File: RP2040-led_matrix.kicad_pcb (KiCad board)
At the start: 2 copper layers, 187 parts, among them J2 USB_C_Receptacle, Q1 BSS84, Q10 BSS84, Q11 2N7002, Q12 2N7002, Q13 2N7002, Q14 2N7002, Q15 2N7002, Q16 2N7002, Q17 2N7002, Q18 2N7002, Q19 2N7002, Q2 BSS84, Q20 2N7002, Q3 BSS84, Q4 BSS84, Q5 BSS84, Q6 BSS84, Q7 BSS84, Q8 BSS84, Q9 BSS84, SW2 SW_DIP_x01, U1 W25Q16JVSS, U2 RP2040, U4 NCP1117-1.5_SOT223, Y2 ABM8-272-T3

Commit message: improved design of the matrix
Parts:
- removed C17, C18: 100n, Capacitor_SMD:C_0603_1608Metric
- removed J2: USB_C_Receptacle, Connector_USB:USB_C_Receptacle_GCT_USB4110
- removed SW2: SW_DIP_x01, Button_Switch_SMD:SW_DIP_SPSTx01_Slide_6.7x4.1mm_W6.73mm_P2.54mm_LowProfile_JPin
- removed U4: NCP1117-1.5_SOT223, Package_TO_SOT_SMD:SOT-223-3_TabPin2
- removed Y2: ABM8-272-T3, Crystal:Crystal_SMD_3225-4Pin_3.2x2.5mm
- added C1: 15p, Capacitor_SMD:C_0603_1608Metric, F.Cu at (117.7, 16.4)
- added C2: 15p, Capacitor_SMD:C_0603_1608Metric, F.Cu at (117.7, 18.9)
- added J1: USB_C_Receptacle, Connector_USB:USB_C_Receptacle_GCT_USB4110, F.Cu at (165.0, 50.0)
- added R46: 100, Resistor_SMD:R_0603_1608Metric, F.Cu at (101.7, 16.9)
- added R47: 100, Resistor_SMD:R_0603_1608Metric, F.Cu at (101.7, 19.4)
- added R48: 100, Resistor_SMD:R_0603_1608Metric, F.Cu at (101.7, 21.9)
- added R49: 100, Resistor_SMD:R_0603_1608Metric, F.Cu at (101.7, 24.4)
- added R50: 100, Resistor_SMD:R_0603_1608Metric, F.Cu at (101.7, 27.0)
- added R51: 100, Resistor_SMD:R_0603_1608Metric, F.Cu at (101.7, 29.5)
- added R52: 100, Resistor_SMD:R_0603_1608Metric, F.Cu at (101.7, 32.0)
- added R53: 100, Resistor_SMD:R_0603_1608Metric, F.Cu at (101.7, 34.5)
- added R54: 100, Resistor_SMD:R_0603_1608Metric, F.Cu at (101.7, 37.0)
- added R55: 100, Resistor_SMD:R_0603_1608Metric, F.Cu at (101.7, 39.5)
- added SW1: SW_DIP_x01, Button_Switch_SMD:SW_DIP_SPSTx01_Slide_6.7x4.1mm_W6.73mm_P2.54mm_LowProfile_JPin, F.Cu at (176.0, 63.0)
- added U3: W25Q16JVSS, Package_SO:SOIC-8_5.3x5.3mm_P1.27mm, F.Cu at (152.5, 63.0)
- added Y1: ABM8-272-T3, Crystal:Crystal_SMD_3225-4Pin_3.2x2.5mm, F.Cu at (174.4, 74.3)
- C10, C9: value 10u -> 100n
- C13, C14, C15: value 100n -> 10u
- C3: value 1u -> 10u
- C4: value 1u -> 100n
- C6, C7: value 15p -> 100n
- R1: value 1k -> 5.1k
- R12, R18, R24, R33: value 100 -> 47
- R13, R19, R25, R28, R31, R34: value 100k -> 100
- R14, R20, R26, R29, R32, R36, R37, R40, R41, R44, R45, R8: value 100 -> 100k
- R15, R21, R27, R30, R9: value 100k -> 47
- R2: value 100 -> 5.1k
- R3: value 100k -> 1k
- R4: value 10k -> 1k
- R5: value 1k -> 100k
- R6: value 5.1k -> 47
- R7: value 5.1k -> 100
- U1: value W25Q16JVSS -> RP2040; footprint Package_SO:SOIC-8_5.3x5.3mm_P1.27mm -> Package_DFN_QFN:QFN-56-1EP_7x7mm_P0.4mm_EP3.2x3.2mm
- U2: value RP2040 -> NCP1117-1.5_SOT223; footprint Package_DFN_QFN:QFN-56-1EP_7x7mm_P0.4mm_EP3.2x3.2mm -> Package_TO_SOT_SMD:SOT-223-3_TabPin2
- moved R6 103.6 mm to (85.6, 16.9)
- moved R7 103.6 mm to (85.6, 19.4)
- moved D1 87.6 mm to (30.0, 25.8)
- moved D10 87.6 mm to (30.0, 49.1)
- moved D100 87.6 mm to (58.3, 46.5)
- moved D11 87.6 mm to (30.0, 51.7)
- moved D12 87.6 mm to (30.0, 54.3)
- moved D13 87.6 mm to (30.0, 56.9)
- moved D14 87.6 mm to (34.0, 25.8)
- moved D15 87.6 mm to (34.0, 28.4)
- moved D16 87.6 mm to (34.0, 31.0)
- moved D17 87.6 mm to (34.0, 33.6)
- moved D18 87.6 mm to (34.0, 36.2)
- moved D19 87.6 mm to (34.0, 38.7)
- moved D2 87.6 mm to (30.0, 28.4)
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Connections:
- C14 pad 1: +3.3V -> +5V
- C16 pad 1: +3.3V -> GND
- C16 pad 2: GND -> +3.3V
- C3 pad 1: +3.3V -> GND
- C3 pad 2: GND -> +1V1
- C6 pad 1: Net-(U2-XIN) -> +3.3V
- C7 pad 1: Net-(C7-Pad1) -> +3.3V
- C8 pad 1: GND -> +3.3V
- C8 pad 2: +3.3V -> GND
- C9 pad 1: +5V -> +3.3V
- Q1 pad 2: +5V -> Net-(Q1-S)
- Q10 pad 2: +5V -> Net-(Q10-S)
- Q2 pad 2: +5V -> Net-(Q2-S)
- Q3 pad 2: +5V -> Net-(Q3-S)
- Q4 pad 2: +5V -> Net-(Q4-S)
- Q5 pad 2: +5V -> Net-(Q5-S)
- Q6 pad 2: +5V -> Net-(Q6-S)
- Q7 pad 2: +5V -> Net-(Q7-S)
- Q8 pad 2: +5V -> Net-(Q8-S)
- Q9 pad 2: +5V -> Net-(Q9-S)
- R1 pad 2: /QSPI_SS -> GND
- R10 pad 1: C3 -> C2
- R10 pad 2: Net-(Q3-G) -> Net-(Q2-G)
- R11 pad 1: Net-(Q3-G) -> Net-(Q2-G)
- R11 pad 2: +5V -> Net-(Q2-S)
- R12 pad 1: R1 -> +3.3V
- R12 pad 2: Net-(Q11-G) -> Net-(Q3-S)
- R13 pad 1: Net-(Q11-G) -> C3
- R13 pad 2: GND -> Net-(Q3-G)
- R14 pad 1: C4 -> Net-(Q3-G)
- R14 pad 2: Net-(Q4-G) -> Net-(Q3-S)
- R15 pad 1: Net-(Q4-G) -> +3.3V
- R15 pad 2: +5V -> Net-(Q4-S)
- R16 pad 1: C5 -> C4
- R16 pad 2: Net-(Q5-G) -> Net-(Q4-G)
- R17 pad 1: Net-(Q5-G) -> Net-(Q4-G)
- R17 pad 2: +5V -> Net-(Q4-S)
- R18 pad 1: C6 -> +3.3V
- R18 pad 2: Net-(Q6-G) -> Net-(Q5-S)
- R19 pad 1: Net-(Q6-G) -> C5
- R19 pad 2: +5V -> Net-(Q5-G)
- R2 pad 1: C1 -> Net-(J1-CC2)
- R2 pad 2: Net-(Q1-G) -> GND
- R20 pad 1: C7 -> Net-(Q5-G)
- R20 pad 2: Net-(Q7-G) -> Net-(Q5-S)
- R21 pad 1: Net-(Q7-G) -> +3.3V
- R21 pad 2: +5V -> Net-(Q6-S)
- R22 pad 1: C8 -> C6
- R22 pad 2: Net-(Q8-G) -> Net-(Q6-G)
- R23 pad 1: Net-(Q8-G) -> Net-(Q6-G)
- R23 pad 2: +5V -> Net-(Q6-S)
- R24 pad 1: C9 -> +3.3V
- R24 pad 2: Net-(Q9-G) -> Net-(Q7-S)
- R25 pad 1: Net-(Q9-G) -> C7
- R25 pad 2: +5V -> Net-(Q7-G)
- R26 pad 1: C10 -> Net-(Q7-G)
- R26 pad 2: Net-(Q10-G) -> Net-(Q7-S)
- R27 pad 1: Net-(Q10-G) -> +3.3V
- R27 pad 2: +5V -> Net-(Q8-S)
- R28 pad 1: Net-(Q12-G) -> C8
- R28 pad 2: GND -> Net-(Q8-G)
- R29 pad 1: R2 -> Net-(Q8-G)
- R29 pad 2: Net-(Q12-G) -> Net-(Q8-S)
- R3 pad 1: Net-(Q1-G) -> Net-(U1-XOUT)
- R3 pad 2: +5V -> Net-(C2-Pad1)
- R30 pad 1: Net-(Q13-G) -> +3.3V
- R30 pad 2: GND -> Net-(Q9-S)
- R31 pad 1: Net-(Q14-G) -> C9
- R31 pad 2: GND -> Net-(Q9-G)
- R32 pad 1: R3 -> Net-(Q9-G)
- R32 pad 2: Net-(Q13-G) -> Net-(Q9-S)
- R33 pad 1: R4 -> +3.3V
- R33 pad 2: Net-(Q14-G) -> Net-(Q10-S)
- R34 pad 1: Net-(Q15-G) -> C10
- R34 pad 2: GND -> Net-(Q10-G)
- R35 pad 1: Net-(Q16-G) -> Net-(Q10-G)
- R35 pad 2: GND -> Net-(Q10-S)
- R36 pad 1: R5 -> Net-(Q11-G)
- R36 pad 2: Net-(Q15-G) -> GND
- R37 pad 1: R6 -> Net-(Q12-G)
- R37 pad 2: Net-(Q16-G) -> GND
- R38 pad 1: Net-(Q17-G) -> Net-(Q13-G)
- R39 pad 1: Net-(Q18-G) -> Net-(Q14-G)
- R4 pad 1: /QSPI_SS -> Net-(R4-Pad1)
- R4 pad 2: +3.3V -> /QSPI_SS
- R40 pad 1: R7 -> Net-(Q15-G)
- R40 pad 2: Net-(Q17-G) -> GND
- R41 pad 1: R8 -> Net-(Q16-G)
- R41 pad 2: Net-(Q18-G) -> GND
- R42 pad 1: Net-(Q19-G) -> Net-(Q17-G)
- R43 pad 1: Net-(Q20-G) -> Net-(Q18-G)
- R44 pad 1: R9 -> Net-(Q19-G)
- R44 pad 2: Net-(Q19-G) -> GND
- R45 pad 1: R10 -> Net-(Q20-G)
- R45 pad 2: Net-(Q20-G) -> GND
- R5 pad 1: Net-(U2-XOUT) -> /QSPI_SS
- R5 pad 2: Net-(C7-Pad1) -> +3.3V
- R6 pad 1: Net-(J2-CC1) -> +3.3V
- R6 pad 2: GND -> Net-(Q1-S)
- R7 pad 1: Net-(J2-CC2) -> C1
- R7 pad 2: GND -> Net-(Q1-G)
- R8 pad 1: C2 -> Net-(Q1-G)
- R8 pad 2: Net-(Q2-G) -> Net-(Q1-S)
- R9 pad 1: Net-(Q2-G) -> +3.3V
- R9 pad 2: +5V -> Net-(Q2-S)
- U1 pad 1: /QSPI_SS -> +3.3V
- U1 pad 2: /QSPI_SD1 -> unconnected-(U1-GPIO0-Pad2)
- U1 pad 3: /QSPI_SD2 -> C1
- U1 pad 4: GND -> C2
- U1 pad 5: /QSPI_SD0 -> C3
- U1 pad 6: /QSPI_SCLK -> C4
- U1 pad 7: /QSPI_SD3 -> C5
- U1 pad 8: +3.3V -> C6
- U2 pad 1: +3.3V -> GND
- U2 pad 2: unconnected-(U2-GPIO0-Pad2) -> +3.3V
- U2 pad 3: C1 -> +5V

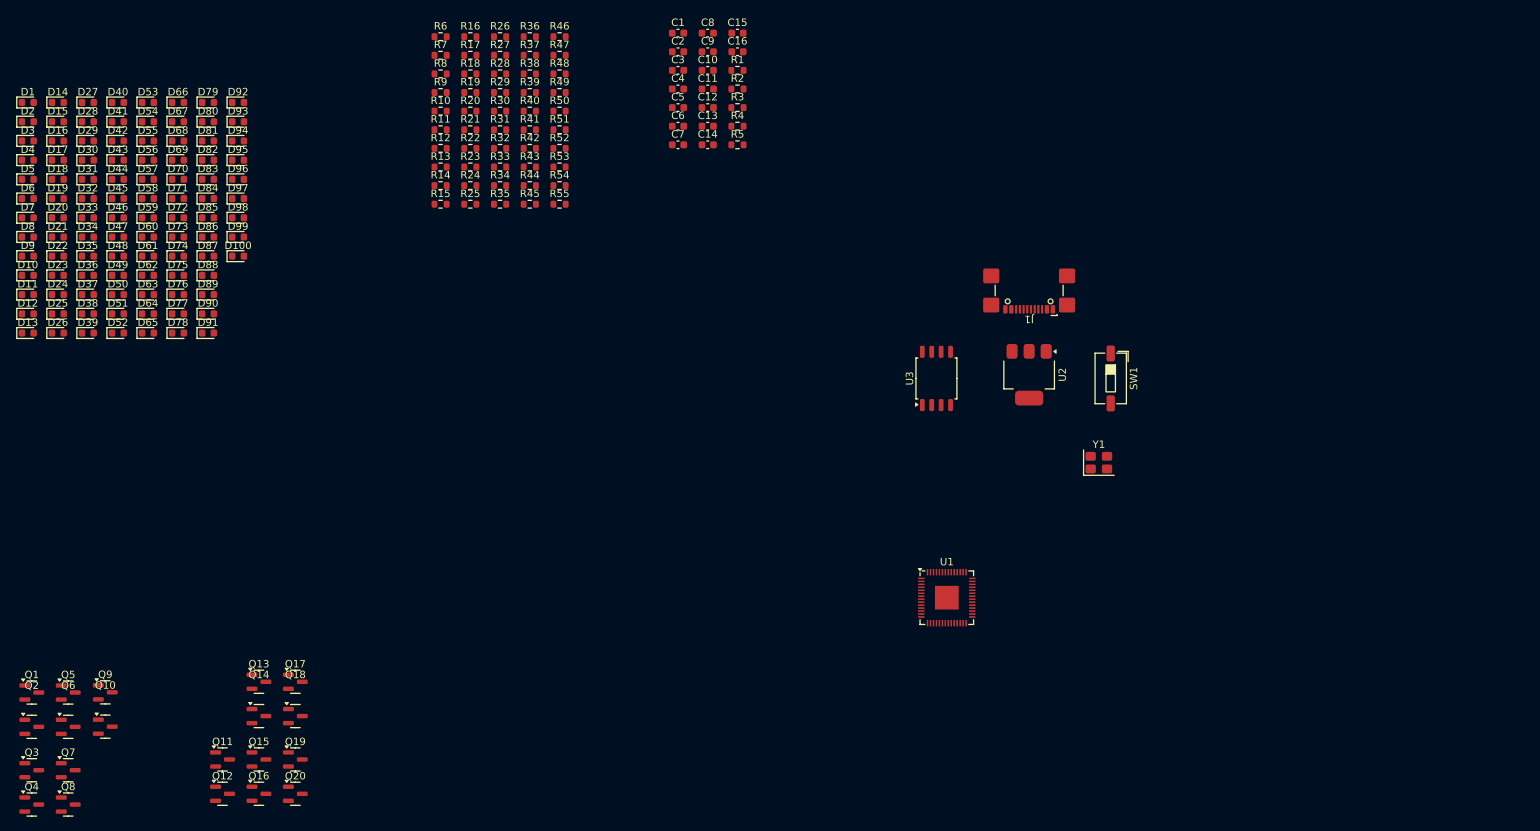
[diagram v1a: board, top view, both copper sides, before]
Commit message: improved design and starting to layout the components
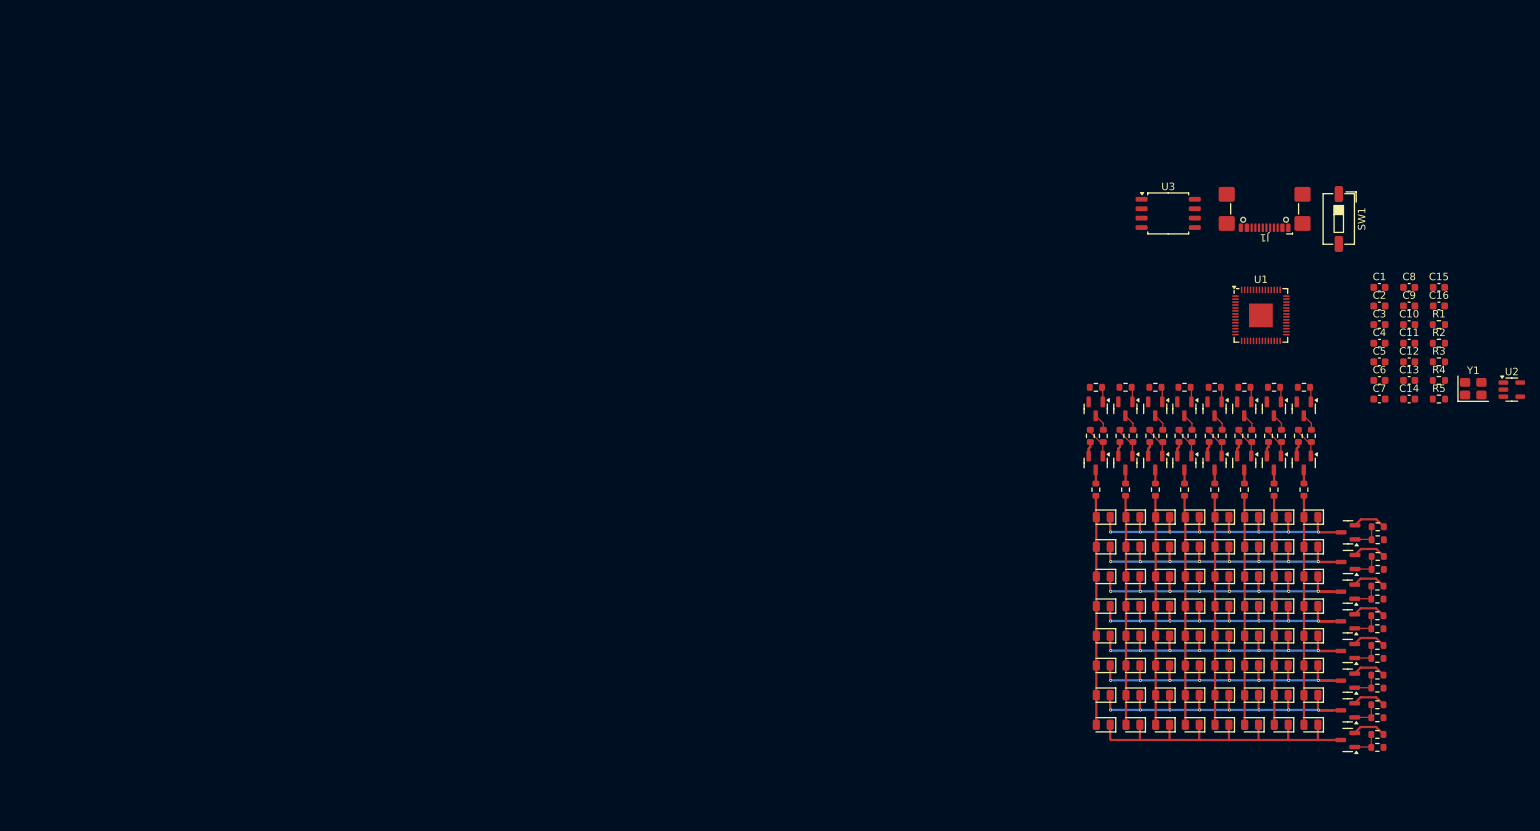
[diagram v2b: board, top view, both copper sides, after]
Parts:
- removed D100, D65, D66, D67, D68, D69, D70, D71, D72, D73, D74, D75, D76, D77, D78, D79, D80, D81, D82, D83, D84, D85, D86, D87, D88, D89, D90, D91, D92, D93, D94, D95, D96, D97, D98, D99: LED_45deg, LED_SMD:LED_0603_1608Metric
- removed R54, R55: 100, Resistor_SMD:R_0603_1608Metric
- added Q21: 2N7002, Package_TO_SOT_SMD:SOT-23, F.Cu at (208.0, 103.8)
- added Q22: 2N7002, Package_TO_SOT_SMD:SOT-23, F.Cu at (208.0, 107.8)
- added Q23: 2N7002, Package_TO_SOT_SMD:SOT-23, F.Cu at (208.0, 111.8)
- added Q24: 2N7002, Package_TO_SOT_SMD:SOT-23, F.Cu at (208.0, 83.8)
- C1: value 15p -> 10u
- C11, C16: value 100n -> 10u
- C12: value 100n -> 15p
- C13: value 10u -> 15p
- C15, C3: value 10u -> 100n
- C2: value 15p -> 100n
- D1, D10, D11, D12, D13, D14, D15, D16, D17, D18, D19, D2, D20, D21, D22, D23, D24, D25, D26, D27, D28, D29, D3, D30, D31, D32, D33, D34, D35, D36, D37, D38, D39, D4, D40, D41, D42, D43, D44, D45, D46, D47, D48, D49, D5, D50, D51, D52, D53, D54, D55, D56, D57, D58, D59, D6, D60, D61, D62, D63, D64, D7, D8, D9: footprint LED_SMD:LED_0603_1608Metric -> LED_SMD:LED_0805_2012Metric
- Q10, Q5: value BSS84 -> 2N7002
- Q12, Q14, Q16, Q18: value 2N7002 -> BSS84
- Q13, Q15, Q17, Q19: value 2N7002 -> BC817
- Q2, Q4, Q7, Q9: value BSS84 -> BC817
- R1: value 5.1k -> 1k
- R10, R16, R28: value 100 -> 47
- R11, R14, R17, R23, R26, R29, R35, R37, R39, R41, R43, R44: value 100k -> 10k
- R12, R15, R18, R27, R30: value 47 -> 100
- R13, R19, R31, R46, R48, R50, R52, R7: value 100 -> 10k
- R20, R32, R36, R40: value 100k -> 47
- R21, R24, R33, R9: value 47 -> 10k
- R3: value 1k -> 5.1k
- R38, R42, R45, R8: value 100k -> 100
- U2: value NCP1117-1.5_SOT223 -> MIC5504-3.3YM5; footprint Package_TO_SOT_SMD:SOT-223-3_TabPin2 -> Package_TO_SOT_SMD:SOT-23-5
- moved Q5 173.5 mm to (208.0, 87.8), turned to 180 degrees
- moved D40 170.9 mm to (191.0, 109.7), turned to 180 degrees
- moved D56 170.7 mm to (199.0, 109.7), turned to 180 degrees
- moved D55 170.1 mm to (199.0, 105.7), turned to 180 degrees
- moved D54 169.5 mm to (199.0, 101.7), turned to 180 degrees
- moved D53 168.9 mm to (199.0, 97.7), turned to 180 degrees
- moved Q10 168.5 mm to (208.0, 91.8), turned to 180 degrees
- moved D64 166.3 mm to (203.0, 109.7), turned to 180 degrees
- moved D63 165.8 mm to (203.0, 105.7), turned to 180 degrees
- moved D48 165.4 mm to (195.0, 109.7), turned to 180 degrees
- moved D62 165.4 mm to (203.0, 101.7), turned to 180 degrees
- moved D16 165.0 mm to (179.0, 109.7), turned to 180 degrees
- moved D61 164.9 mm to (203.0, 97.7), turned to 180 degrees
- moved D32 164.9 mm to (187.0, 109.7), turned to 180 degrees
- moved D47 164.9 mm to (195.0, 105.7), turned to 180 degrees
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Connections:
- net R6 renamed /r8
- C1 pad 1: Net-(U1-XIN) -> GND
- C1 pad 2: GND -> +1V1
- C12 pad 1: +3.3V -> /XIN
- C13 pad 1: +3.3V -> Net-(C13-Pad1)
- C15 pad 1: +3.3V -> GND
- C15 pad 2: GND -> +3.3V
- C16 pad 1: GND -> +3.3V
- C16 pad 2: +3.3V -> GND
- C2 pad 1: Net-(C2-Pad1) -> GND
- C2 pad 2: GND -> +1V1
- C4 pad 1: GND -> +3.3V
- C4 pad 2: +1V1 -> GND
- C5 pad 1: GND -> +3.3V
- C5 pad 2: +1V1 -> GND
- D1 pad 1: /Led Matrix/C0 -> /Led Matrix/Lowside1/V_led-
- D1 pad 2: Net-(D1-A) -> /Led Matrix/Highside1/V_led+
- D10 pad 1: /Led Matrix/C0 -> /Led Matrix/Lowside2/V_led-
- D10 pad 2: Net-(D1-A) -> /Led Matrix/Highside2/V_led+
- D11 pad 1: /Led Matrix/C0 -> /Led Matrix/Lowside3/V_led-
- D11 pad 2: Net-(D11-A) -> /Led Matrix/Highside2/V_led+
- D12 pad 1: /Led Matrix/C0 -> /Led Matrix/Lowside4/V_led-
- D12 pad 2: Net-(D11-A) -> /Led Matrix/Highside2/V_led+
- D13 pad 1: /Led Matrix/C0 -> /Led Matrix/Lowside5/V_led-
- D13 pad 2: Net-(D11-A) -> /Led Matrix/Highside2/V_led+
- D14 pad 1: /Led Matrix/C0 -> /Led Matrix/Lowside6/V_led-
- D14 pad 2: Net-(D11-A) -> /Led Matrix/Highside2/V_led+
- D15 pad 1: /Led Matrix/C0 -> /Led Matrix/Lowside7/V_led-
- D15 pad 2: Net-(D11-A) -> /Led Matrix/Highside2/V_led+
- D16 pad 1: /Led Matrix/C0 -> /Led Matrix/Lowside8/V_led-
- D16 pad 2: Net-(D11-A) -> /Led Matrix/Highside2/V_led+
- D17 pad 1: /Led Matrix/C0 -> /Led Matrix/Lowside1/V_led-
- D17 pad 2: Net-(D11-A) -> /Led Matrix/Highside3/V_led+
- D18 pad 1: /Led Matrix/C0 -> /Led Matrix/Lowside2/V_led-
- D18 pad 2: Net-(D11-A) -> /Led Matrix/Highside3/V_led+
- D19 pad 1: /Led Matrix/C0 -> /Led Matrix/Lowside3/V_led-
- D19 pad 2: Net-(D11-A) -> /Led Matrix/Highside3/V_led+
- D2 pad 1: /Led Matrix/C0 -> /Led Matrix/Lowside2/V_led-
- D2 pad 2: Net-(D1-A) -> /Led Matrix/Highside1/V_led+
- D20 pad 1: /Led Matrix/C0 -> /Led Matrix/Lowside4/V_led-
- D20 pad 2: Net-(D11-A) -> /Led Matrix/Highside3/V_led+
- D21 pad 1: /Led Matrix/C0 -> /Led Matrix/Lowside5/V_led-
- D21 pad 2: Net-(D21-A) -> /Led Matrix/Highside3/V_led+
- D22 pad 1: /Led Matrix/C0 -> /Led Matrix/Lowside6/V_led-
- D22 pad 2: Net-(D21-A) -> /Led Matrix/Highside3/V_led+
- D23 pad 1: /Led Matrix/C0 -> /Led Matrix/Lowside7/V_led-
- D23 pad 2: Net-(D21-A) -> /Led Matrix/Highside3/V_led+
- D24 pad 1: /Led Matrix/C0 -> /Led Matrix/Lowside8/V_led-
- D24 pad 2: Net-(D21-A) -> /Led Matrix/Highside3/V_led+
- D25 pad 1: /Led Matrix/C0 -> /Led Matrix/Lowside1/V_led-
- D25 pad 2: Net-(D21-A) -> /Led Matrix/Highside4/V_led+
- D26 pad 1: /Led Matrix/C0 -> /Led Matrix/Lowside2/V_led-
- D26 pad 2: Net-(D21-A) -> /Led Matrix/Highside4/V_led+
- D27 pad 1: /Led Matrix/C0 -> /Led Matrix/Lowside3/V_led-
- D27 pad 2: Net-(D21-A) -> /Led Matrix/Highside4/V_led+
- D28 pad 1: /Led Matrix/C0 -> /Led Matrix/Lowside4/V_led-
- D28 pad 2: Net-(D21-A) -> /Led Matrix/Highside4/V_led+
- D29 pad 1: /Led Matrix/C0 -> /Led Matrix/Lowside5/V_led-
- D29 pad 2: Net-(D21-A) -> /Led Matrix/Highside4/V_led+
- D3 pad 1: /Led Matrix/C0 -> /Led Matrix/Lowside3/V_led-
- D3 pad 2: Net-(D1-A) -> /Led Matrix/Highside1/V_led+
- D30 pad 1: /Led Matrix/C0 -> /Led Matrix/Lowside6/V_led-
- D30 pad 2: Net-(D21-A) -> /Led Matrix/Highside4/V_led+
- D31 pad 1: /Led Matrix/C0 -> /Led Matrix/Lowside7/V_led-
- D31 pad 2: Net-(D31-A) -> /Led Matrix/Highside4/V_led+
- D32 pad 1: /Led Matrix/C0 -> /Led Matrix/Lowside8/V_led-
- D32 pad 2: Net-(D31-A) -> /Led Matrix/Highside4/V_led+
- D33 pad 1: /Led Matrix/C0 -> /Led Matrix/Lowside1/V_led-
- D33 pad 2: Net-(D31-A) -> /Led Matrix/Highside5/V_led+
- D34 pad 1: /Led Matrix/C0 -> /Led Matrix/Lowside2/V_led-
- D34 pad 2: Net-(D31-A) -> /Led Matrix/Highside5/V_led+
- D35 pad 1: /Led Matrix/C0 -> /Led Matrix/Lowside3/V_led-
- D35 pad 2: Net-(D31-A) -> /Led Matrix/Highside5/V_led+
- D36 pad 1: /Led Matrix/C0 -> /Led Matrix/Lowside4/V_led-
- D36 pad 2: Net-(D31-A) -> /Led Matrix/Highside5/V_led+
- D37 pad 1: /Led Matrix/C0 -> /Led Matrix/Lowside5/V_led-
- D37 pad 2: Net-(D31-A) -> /Led Matrix/Highside5/V_led+
- D38 pad 1: /Led Matrix/C0 -> /Led Matrix/Lowside6/V_led-
- D38 pad 2: Net-(D31-A) -> /Led Matrix/Highside5/V_led+
- D39 pad 1: /Led Matrix/C0 -> /Led Matrix/Lowside7/V_led-
- D39 pad 2: Net-(D31-A) -> /Led Matrix/Highside5/V_led+
- D4 pad 1: /Led Matrix/C0 -> /Led Matrix/Lowside4/V_led-
- D4 pad 2: Net-(D1-A) -> /Led Matrix/Highside1/V_led+
- D40 pad 1: /Led Matrix/C0 -> /Led Matrix/Lowside8/V_led-
- D40 pad 2: Net-(D31-A) -> /Led Matrix/Highside5/V_led+
- D41 pad 1: /Led Matrix/C0 -> /Led Matrix/Lowside1/V_led-
- D41 pad 2: Net-(D41-A) -> /Led Matrix/Highside6/V_led+
- D42 pad 1: /Led Matrix/C0 -> /Led Matrix/Lowside2/V_led-
- D42 pad 2: Net-(D41-A) -> /Led Matrix/Highside6/V_led+
- D43 pad 1: /Led Matrix/C0 -> /Led Matrix/Lowside3/V_led-
- D43 pad 2: Net-(D41-A) -> /Led Matrix/Highside6/V_led+
- D44 pad 1: /Led Matrix/C0 -> /Led Matrix/Lowside4/V_led-
- D44 pad 2: Net-(D41-A) -> /Led Matrix/Highside6/V_led+
- D45 pad 1: /Led Matrix/C0 -> /Led Matrix/Lowside5/V_led-
- D45 pad 2: Net-(D41-A) -> /Led Matrix/Highside6/V_led+
- D46 pad 1: /Led Matrix/C0 -> /Led Matrix/Lowside6/V_led-
- D46 pad 2: Net-(D41-A) -> /Led Matrix/Highside6/V_led+
- D47 pad 1: /Led Matrix/C0 -> /Led Matrix/Lowside7/V_led-
- D47 pad 2: Net-(D41-A) -> /Led Matrix/Highside6/V_led+
- D48 pad 1: /Led Matrix/C0 -> /Led Matrix/Lowside8/V_led-
- D48 pad 2: Net-(D41-A) -> /Led Matrix/Highside6/V_led+
- D49 pad 1: /Led Matrix/C0 -> /Led Matrix/Lowside1/V_led-
- D49 pad 2: Net-(D41-A) -> /Led Matrix/Highside7/V_led+
- D5 pad 1: /Led Matrix/C0 -> /Led Matrix/Lowside5/V_led-
- D5 pad 2: Net-(D1-A) -> /Led Matrix/Highside1/V_led+
- D50 pad 1: /Led Matrix/C0 -> /Led Matrix/Lowside2/V_led-
- D50 pad 2: Net-(D41-A) -> /Led Matrix/Highside7/V_led+
- D51 pad 1: /Led Matrix/C0 -> /Led Matrix/Lowside3/V_led-
- D51 pad 2: Net-(D51-A) -> /Led Matrix/Highside7/V_led+
- D52 pad 1: /Led Matrix/C0 -> /Led Matrix/Lowside4/V_led-
- D52 pad 2: Net-(D51-A) -> /Led Matrix/Highside7/V_led+
- D53 pad 1: /Led Matrix/C0 -> /Led Matrix/Lowside5/V_led-
- D53 pad 2: Net-(D51-A) -> /Led Matrix/Highside7/V_led+
- D54 pad 1: /Led Matrix/C0 -> /Led Matrix/Lowside6/V_led-
- D54 pad 2: Net-(D51-A) -> /Led Matrix/Highside7/V_led+
- D55 pad 1: /Led Matrix/C0 -> /Led Matrix/Lowside7/V_led-
- D55 pad 2: Net-(D51-A) -> /Led Matrix/Highside7/V_led+
- D56 pad 1: /Led Matrix/C0 -> /Led Matrix/Lowside8/V_led-
- D56 pad 2: Net-(D51-A) -> /Led Matrix/Highside7/V_led+
- D57 pad 1: /Led Matrix/C0 -> /Led Matrix/Lowside1/V_led-
- D57 pad 2: Net-(D51-A) -> /Led Matrix/Highside8/V_led+
- D58 pad 1: /Led Matrix/C0 -> /Led Matrix/Lowside2/V_led-
- D58 pad 2: Net-(D51-A) -> /Led Matrix/Highside8/V_led+
- D59 pad 1: /Led Matrix/C0 -> /Led Matrix/Lowside3/V_led-
- D59 pad 2: Net-(D51-A) -> /Led Matrix/Highside8/V_led+
- D6 pad 1: /Led Matrix/C0 -> /Led Matrix/Lowside6/V_led-
- D6 pad 2: Net-(D1-A) -> /Led Matrix/Highside1/V_led+
- D60 pad 1: /Led Matrix/C0 -> /Led Matrix/Lowside4/V_led-
- D60 pad 2: Net-(D51-A) -> /Led Matrix/Highside8/V_led+
- D61 pad 1: /Led Matrix/C0 -> /Led Matrix/Lowside5/V_led-
- D61 pad 2: Net-(D61-A) -> /Led Matrix/Highside8/V_led+
- D62 pad 1: /Led Matrix/C0 -> /Led Matrix/Lowside6/V_led-
- D62 pad 2: Net-(D61-A) -> /Led Matrix/Highside8/V_led+
- D63 pad 1: /Led Matrix/C0 -> /Led Matrix/Lowside7/V_led-
- D63 pad 2: Net-(D61-A) -> /Led Matrix/Highside8/V_led+
- D64 pad 1: /Led Matrix/C0 -> /Led Matrix/Lowside8/V_led-
- D64 pad 2: Net-(D61-A) -> /Led Matrix/Highside8/V_led+
- D7 pad 1: /Led Matrix/C0 -> /Led Matrix/Lowside7/V_led-
- D7 pad 2: Net-(D1-A) -> /Led Matrix/Highside1/V_led+
- D8 pad 1: /Led Matrix/C0 -> /Led Matrix/Lowside8/V_led-
- D8 pad 2: Net-(D1-A) -> /Led Matrix/Highside1/V_led+
- D9 pad 1: /Led Matrix/C0 -> /Led Matrix/Lowside1/V_led-
- D9 pad 2: Net-(D1-A) -> /Led Matrix/Highside2/V_led+
- Q1 pad 2: Net-(Q1-S) -> +5V
- Q1 pad 3: Net-(D1-A) -> Net-(Q1-D)
- Q10 pad 2: Net-(Q10-S) -> GND
- Q10 pad 3: Net-(D100-A) -> /Led Matrix/Lowside3/V_led-
- Q11 pad 3: /Led Matrix/C0 -> /Led Matrix/Lowside4/V_led-
- Q12 pad 2: GND -> +5V
- Q12 pad 3: /Led Matrix/C0 -> Net-(Q12-D)
- Q13 pad 1: Net-(Q13-G) -> Net-(Q13-B)
- Q13 pad 3: /Led Matrix/C0 -> Net-(Q13-C)
- Q14 pad 2: GND -> +5V
- Q14 pad 3: /Led Matrix/C0 -> Net-(Q14-D)
- Q15 pad 1: Net-(Q15-G) -> Net-(Q15-B)
- Q15 pad 3: /Led Matrix/C0 -> Net-(Q15-C)
- Q16 pad 2: GND -> +5V
- Q16 pad 3: /Led Matrix/C0 -> Net-(Q16-D)
- Q17 pad 1: Net-(Q17-G) -> Net-(Q17-B)
- Q17 pad 3: /Led Matrix/C0 -> Net-(Q17-C)
- Q18 pad 2: GND -> +5V
- Q18 pad 3: /Led Matrix/C0 -> Net-(Q18-D)
- Q19 pad 1: Net-(Q19-G) -> Net-(Q19-B)
- Q19 pad 3: /Led Matrix/C0 -> Net-(Q19-C)
- Q2 pad 1: Net-(Q2-G) -> Net-(Q2-B)
- Q2 pad 2: Net-(Q2-S) -> GND
- Q2 pad 3: Net-(D11-A) -> Net-(Q2-C)
- Q20 pad 3: /Led Matrix/C0 -> /Led Matrix/Lowside5/V_led-
- Q3 pad 2: Net-(Q3-S) -> +5V
- Q3 pad 3: Net-(D21-A) -> Net-(Q3-D)
- Q4 pad 1: Net-(Q4-G) -> Net-(Q4-B)
- Q4 pad 2: Net-(Q4-S) -> GND
- Q4 pad 3: Net-(D31-A) -> Net-(Q4-C)
- Q5 pad 2: Net-(Q5-S) -> GND
- Q5 pad 3: Net-(D41-A) -> /Led Matrix/Lowside2/V_led-
- Q6 pad 2: Net-(Q6-S) -> +5V
- Q6 pad 3: Net-(D51-A) -> Net-(Q6-D)
- Q7 pad 1: Net-(Q7-G) -> Net-(Q7-B)
- Q7 pad 2: Net-(Q7-S) -> GND
- Q7 pad 3: Net-(D61-A) -> Net-(Q7-C)
- Q8 pad 2: Net-(Q8-S) -> +5V
- Q8 pad 3: Net-(D71-A) -> Net-(Q8-D)
- Q9 pad 1: Net-(Q9-G) -> Net-(Q9-B)
- Q9 pad 2: Net-(Q9-S) -> GND
- Q9 pad 3: Net-(D81-A) -> Net-(Q9-C)
- R1 pad 1: Net-(J1-CC1) -> /XOUT
- R1 pad 2: GND -> Net-(C13-Pad1)
- R10 pad 1: C2 -> Net-(Q3-D)
- R10 pad 2: Net-(Q2-G) -> /Led Matrix/Highside2/V_led+
- R11 pad 1: Net-(Q2-G) -> +5V
- R11 pad 2: Net-(Q2-S) -> Net-(Q3-G)
- R12 pad 1: +3.3V -> Net-(Q3-G)
- R12 pad 2: Net-(Q3-S) -> Net-(Q4-C)
- R13 pad 1: C3 -> /c2
- R13 pad 2: Net-(Q3-G) -> Net-(Q4-B)
- R14 pad 1: Net-(Q3-G) -> Net-(Q5-G)
- R14 pad 2: Net-(Q3-S) -> GND
- R15 pad 1: +3.3V -> /r2
- R15 pad 2: Net-(Q4-S) -> Net-(Q5-G)
- R16 pad 1: C4 -> Net-(Q6-D)
- R16 pad 2: Net-(Q4-G) -> /Led Matrix/Highside3/V_led+
- R17 pad 1: Net-(Q4-G) -> +5V
- R17 pad 2: Net-(Q4-S) -> Net-(Q6-G)
- R18 pad 1: +3.3V -> Net-(Q6-G)
- R18 pad 2: Net-(Q5-S) -> Net-(Q7-C)
- R19 pad 1: C5 -> /c3
- R19 pad 2: Net-(Q5-G) -> Net-(Q7-B)
- R2 pad 1: Net-(J1-CC2) -> Net-(J1-CC1)
- R20 pad 1: Net-(Q5-G) -> Net-(Q8-D)
- R20 pad 2: Net-(Q5-S) -> /Led Matrix/Highside4/V_led+
- R21 pad 1: +3.3V -> +5V
- R21 pad 2: Net-(Q6-S) -> Net-(Q8-G)
- R22 pad 1: C6 -> Net-(Q8-G)
- R22 pad 2: Net-(Q6-G) -> Net-(Q9-C)
- R23 pad 1: Net-(Q6-G) -> /c4
- R23 pad 2: Net-(Q6-S) -> Net-(Q9-B)
- R24 pad 1: +3.3V -> Net-(Q10-G)
- R24 pad 2: Net-(Q7-S) -> GND
- R25 pad 1: C7 -> /r3
- R25 pad 2: Net-(Q7-G) -> Net-(Q10-G)
- R26 pad 1: Net-(Q7-G) -> Net-(Q11-G)
- R26 pad 2: Net-(Q7-S) -> GND
- R27 pad 1: +3.3V -> /r4
- R27 pad 2: Net-(Q8-S) -> Net-(Q11-G)
- R28 pad 1: C8 -> Net-(Q12-D)
- R28 pad 2: Net-(Q8-G) -> /Led Matrix/Highside5/V_led+
- R29 pad 1: Net-(Q8-G) -> +5V
- R29 pad 2: Net-(Q8-S) -> Net-(Q12-G)
- R3 pad 1: Net-(U1-XOUT) -> Net-(J1-CC2)
- R3 pad 2: Net-(C2-Pad1) -> GND
- R30 pad 1: +3.3V -> Net-(Q12-G)
- R30 pad 2: Net-(Q9-S) -> Net-(Q13-C)
- R31 pad 1: C9 -> /c5
- R31 pad 2: Net-(Q9-G) -> Net-(Q13-B)
- R32 pad 1: Net-(Q9-G) -> Net-(Q14-D)
- R32 pad 2: Net-(Q9-S) -> /Led Matrix/Highside6/V_led+
- R33 pad 1: +3.3V -> +5V
- R33 pad 2: Net-(Q10-S) -> Net-(Q14-G)
- R34 pad 1: C10 -> Net-(Q14-G)
- R34 pad 2: Net-(Q10-G) -> Net-(Q15-C)
- R35 pad 1: Net-(Q10-G) -> /c6
- R35 pad 2: Net-(Q10-S) -> Net-(Q15-B)
- R36 pad 1: Net-(Q11-G) -> Net-(Q16-D)
- R36 pad 2: GND -> /Led Matrix/Highside7/V_led+
- R37 pad 1: Net-(Q12-G) -> +5V
- R37 pad 2: GND -> Net-(Q16-G)
- R38 pad 1: Net-(Q13-G) -> Net-(Q16-G)
- R38 pad 2: GND -> Net-(Q17-C)
- R39 pad 1: Net-(Q14-G) -> /c7
- R39 pad 2: GND -> Net-(Q17-B)
- R40 pad 1: Net-(Q15-G) -> Net-(Q18-D)
- R40 pad 2: GND -> /Led Matrix/Highside8/V_led+
- R41 pad 1: Net-(Q16-G) -> +5V
- R41 pad 2: GND -> Net-(Q18-G)
- R42 pad 1: Net-(Q17-G) -> Net-(Q18-G)
- R42 pad 2: GND -> Net-(Q19-C)
- R43 pad 1: Net-(Q18-G) -> /c8
- R43 pad 2: GND -> Net-(Q19-B)
- R44 pad 1: Net-(Q19-G) -> Net-(Q20-G)
- R45 pad 1: Net-(Q20-G) -> /r5
- R45 pad 2: GND -> Net-(Q20-G)
- R46 pad 1: R1 -> Net-(Q21-G)
- R46 pad 2: Net-(Q11-G) -> GND
- R47 pad 1: R2 -> /r6
- R47 pad 2: Net-(Q12-G) -> Net-(Q21-G)
- R48 pad 1: R3 -> Net-(Q22-G)
- R48 pad 2: Net-(Q13-G) -> GND
- R49 pad 1: R4 -> /r7
- R49 pad 2: Net-(Q14-G) -> Net-(Q22-G)
- R50 pad 1: R5 -> Net-(Q23-G)
- R50 pad 2: Net-(Q15-G) -> GND
- R51 pad 2: Net-(Q16-G) -> Net-(Q23-G)
- R52 pad 1: R7 -> Net-(Q24-G)
- R52 pad 2: Net-(Q17-G) -> GND
- R53 pad 1: R8 -> /r1
- R53 pad 2: Net-(Q18-G) -> Net-(Q24-G)
- R6 pad 1: +3.3V -> Net-(Q1-D)
- R6 pad 2: Net-(Q1-S) -> /Led Matrix/Highside1/V_led+
- R7 pad 1: C1 -> +5V
- R8 pad 2: Net-(Q1-S) -> Net-(Q2-C)
- R9 pad 1: +3.3V -> /c1
- R9 pad 2: Net-(Q2-S) -> Net-(Q2-B)
- U1 pad 11: C8 -> /c8
- U1 pad 12: C9 -> /r1
- U1 pad 13: C10 -> /r2
- U1 pad 14: R1 -> /r3
- U1 pad 15: R2 -> /r4
- U1 pad 16: R3 -> /r5
- U1 pad 17: R4 -> /r6
- U1 pad 18: R5 -> /r7
- U1 pad 20: Net-(U1-XIN) -> /XIN
- U1 pad 21: Net-(U1-XOUT) -> /XOUT
- U1 pad 28: R7 -> unconnected-(U1-GPIO17-Pad28)
- U1 pad 29: R8 -> unconnected-(U1-GPIO18-Pad29)
- U1 pad 3: C1 -> /c1
- U1 pad 30: R9 -> unconnected-(U1-GPIO19-Pad30)
- U1 pad 31: R10 -> unconnected-(U1-GPIO20-Pad31)
- U1 pad 4: C2 -> /c2
- U1 pad 5: C3 -> /c3
- U1 pad 6: C4 -> /c4
- U1 pad 7: C5 -> /c5
- U1 pad 8: C6 -> /c6
- U1 pad 9: C7 -> /c7
- U2 pad 1: GND -> +5V
- U2 pad 2: +3.3V -> GND
- Y1 pad 1: Net-(U1-XIN) -> /XIN
- Y1 pad 3: Net-(C2-Pad1) -> Net-(C13-Pad1)
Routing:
- net /Led Matrix/Lowside7/V_led-: track 0.00 -> 48.5 mm, vias 0 -> 8
- net /Led Matrix/Lowside6/V_led-: track 0.00 -> 48.5 mm, vias 0 -> 8
- net /Led Matrix/Lowside5/V_led-: track 0.00 -> 48.5 mm, vias 0 -> 8
- net /Led Matrix/Lowside4/V_led-: track 0.00 -> 48.5 mm, vias 0 -> 8
- net /Led Matrix/Lowside3/V_led-: track 0.00 -> 48.5 mm, vias 0 -> 8
- net /Led Matrix/Lowside2/V_led-: track 0.00 -> 48.5 mm, vias 0 -> 8
- net /Led Matrix/Lowside1/V_led-: track 0.00 -> 47.2 mm, vias 0 -> 8
- net /Led Matrix/Lowside8/V_led-: track 0.00 -> 46.6 mm
- net GND: track 0.00 -> 37.1 mm
- net /Led Matrix/Highside1/V_led+: track 0.00 -> 30.9 mm
- net /Led Matrix/Highside8/V_led+: track 0.00 -> 30.8 mm
- net /Led Matrix/Highside7/V_led+: track 0.00 -> 30.8 mm
- net /Led Matrix/Highside6/V_led+: track 0.00 -> 30.8 mm
- net /Led Matrix/Highside5/V_led+: track 0.00 -> 30.8 mm
- net /Led Matrix/Highside4/V_led+: track 0.00 -> 30.8 mm
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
